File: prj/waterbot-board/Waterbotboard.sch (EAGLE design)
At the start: 63 parts, among them J1 54602-908LF, J2 54602-908LF, U1 MCP4725A0T-E/CHSOT-23-6_MC-L, U2 R-78E5.0-1.0, U3 PCA9615, U4 PCA9615

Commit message: Added boards
waterbot board, relay board
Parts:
- removed D1: SBR2A40P1-7, openag-diodes:SBR2A40P1-7
- removed D2: APT1608, openag-diodes:APT1608CGCK
- removed F1: (no value), fuse:GSH15
- removed J2: 54602-908LF, openag-connectors:RJ45-DI2C-USB-54602-908LFPTH
- removed R1, R19: 100, openag-resistors:100OHM-RC0603JR-07100RL
- removed R13, R14, R15, R16: 600, openag-resistors:600OHM-RC0603FR-07604RL
- removed R17, R18: 120, openag-resistors:120OHM-RC0603FR-07120RL
- removed RELAY_1: G5LE-14_DC12, relay_2:G5LE-14_DC12
- removed TP1, TP12: PTR1B2,54, testpad:PTR1B2,54
- removed TP28, TP3: TPTP06R, openag-testpads:TPTP06R
- removed U$9: LTV-355T, openag-transistors:LTV-355T
- removed U1: MCP4725A0T-E/CHSOT-23-6_MC-L, openag-dacs:MCP4725A0T-E/CHSOT-23-6_MC-L
- removed U4: PCA9615, openag-buffers:PCA9615DPJ
- added C6, C8: 0.1uF, openag-capacitors:0.1UF-C0603C104K5RACTU
- added C7: 4.7uF, openag-capacitors:4.7UF-CL21A475KBQNNNE
- added D10: APT1608, openag-diodes:APT1608CGCK
- added D11: SMAJ26A, openag-diodes:SMAJ26A-13-F
- added D3, D5, D7, D8, D9: SBR2A40P1-7, openag-diodes:SBR2A40P1-7
- added F2, F3, F4, F5, F6: (no value), fuse:GSH15
- added F8: GSH15, openag-fuses:GSH15
- added F9: Use 5A Fuse, openag-fuses:0217005.MXP
- added J4: PJ-036AH, openag-connectors:BARREL-JACK-PJ-036AH-SMT-TR
- added LSP1, LSP10, LSP11, LSP12, LSP13, LSP14, LSP15, LSP2, LSP3, LSP4, LSP5, LSP6, LSP7, LSP8, LSP9: LSP13, solpad:LSP13
- added R20, R21, R22, R23, R24: 100, openag-resistors:100OHM-RC0603JR-07100RL
- added R34, R36, R37, R38, R39, R40, R41, R42: 1K, openag-resistors:1K-ERJ-PB3D1001V
- added R35: 0 OHM, openag-resistors:0OHM-RC0603JR-070RL
- added RELAY_2, RELAY_3, RELAY_4, RELAY_5, RELAY_6: G5LE-14_DC12, relay_2:G5LE-14_DC12
- added SJ_A1, SJ_A2: (no value), openag-connectors:SOLDERJUMPERREFLOW_NOPASTE
- added TP24, TP25, TP26, TP29, TP30, TP31, TP35, TP36, TP37, TP38, TP39, TP40: TPTP04R, openag-testpads:TPTP04R
- added U$10, U$11, U$12, U$13, U$14: LTV-355T, openag-transistors:LTV-355T
- added U5: DAC5578, openag-dacs:DAC5578SPW
- C5: value 0.1uF -> 4.7uF; device openag-capacitors:0.1UF-C0603C104K5RACTU -> openag-capacitors:4.7UF-CL21A475KBQNNNE
- R2: value 100 -> 1K; device openag-resistors:100OHM-RC0603JR-07100RL -> openag-resistors:1K-ERJ-PB3D1001V
- TP27: value TPTP06R -> TPTP04R; device openag-testpads:TPTP06R -> openag-testpads:TPTP04R
- U$6: AUTHOR Dan Poitrast -> Sebastian
- U$7: TITLE LED-DRV -> Water Bot Control Board; URL github.com/openaginitiative/openag-body/prj/usb-hub -> github.com/openaginitiative/openag-body/prj/
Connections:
- removed net DSCLM_2: J2.DSCLM, R15.2, R17.1, U4.DSCLM
- removed net DSCLP_2: J2.DSCLP, R16.1, R17.2, U4.DSCLP
- removed net DSDAM_2: J2.DSDAM, R13.1, R18.2, U4.DSDAM
- removed net DSDAP_3: J2.DSDAP, R14.2, R18.1, U4.DSDAP
- new net !LDAC!: R35.2, R36.2, TP37.TP, U5.!LDAC!
- new net 24V_IN1: F8.1, J4.1
- new net ADDR0: SJ_A1.2, SJ_A2.2, U5.ADDR0
- new net DAC_!CLR!: R34.2, TP38.TP, U5.!CLR!
- new net DIM1: R37.1, U5.VOUT_G
- new net DIM2: R20.1, R38.1, U5.VOUT_E
- new net DIM3: R21.1, R39.1, U5.VOUT_C
- new net DIM4: R22.1, R40.1, U5.VOUT_A
- new net DIM5: R23.1, R41.1, U5.VOUT_H
- new net DIM6: R24.1, R42.1, U5.VOUT_F
- new net N$42: D3.+, RELAY_2.1, U$10.COLLECTOR
- new net N$44: F2.2, RELAY_2.2
- new net N$45: LSP3.MP, RELAY_2.3
- new net N$46: LSP12.MP, RELAY_6.4
- new net N$47: R20.2, U$10.ANODE
- new net N$48: D5.+, RELAY_3.1, U$11.COLLECTOR
- new net N$49: F3.2, RELAY_3.2
- new net N$50: LSP5.MP, RELAY_3.3
- new net N$51: LSP14.MP, RELAY_5.4
- new net N$52: R21.2, U$11.ANODE
- new net N$53: D7.+, RELAY_4.1, U$12.COLLECTOR
- new net N$54: F4.2, RELAY_4.2
- new net N$55: LSP8.MP, RELAY_4.3
- new net N$57: R22.2, U$12.ANODE
- new net N$58: D8.+, RELAY_5.1, U$13.COLLECTOR
- new net N$59: F5.2, RELAY_5.2
- new net N$60: LSP13.MP, RELAY_5.3
- new net N$61: D10.A, R2.1
- new net N$62: R23.2, U$13.ANODE
- new net N$63: D9.+, RELAY_6.1, U$14.COLLECTOR
- new net N$64: F6.2, RELAY_6.2
- new net N$65: LSP11.MP, RELAY_6.3
- new net N$67: R24.2, U$14.ANODE
- new net N$7: F3.1, LSP6.MP
- new net SCL: TP36.TP, U5.SCL
- new net SDA: TP35.TP, U5.SDA
- net +24V: now also C5.1, C8.1, D11.P$2, D3.-, D5.-, D7.-, D8.-, D9.-, F8.2, R2.2, RELAY_2.5, RELAY_3.5, RELAY_4.5, RELAY_5.5, RELAY_6.5, TP24.TP, TP27.TP, TP29.TP; no longer D1.-, J2.+24V, RELAY_1.5, TP3.TP
- net +3V3: now also C6.1, C7.1, R34.1, R36.1, R37.2, R38.2, R39.2, R40.2, R41.2, R42.2, SJ_A1.1, TP30.TP, U5.AVDD, U5.VREF_IN; no longer U4.VDD_(A)
- net +5V: no longer R14.1, R16.2, TP27.TP, U1.VDD, U4.VDD_(B)
- net 24V_EMI: no longer R1.2
- net GND: now also C5.2, C6.2, C7.2, C8.2, D10.C, D11.P$1, J1.GND, J4.2, J4.3, R35.1, SJ_A2.1, TP25.TP, TP26.TP, TP31.TP, TP39.TP, TP40.TP, U$10.CATHODE, U$10.EMITTER, U$11.CATHODE, U$11.EMITTER, U$12.CATHODE, U$12.EMITTER, U$13.CATHODE, U$13.EMITTER, U$14.CATHODE, U$14.EMITTER, U5.GND; no longer D2.C, R13.2, R15.1, R19.1, TP28.TP, U$9.CATHODE, U$9.EMITTER, U1.VSS, U4.VSS
- net N$11: now also F4.1, LSP9.MP; no longer F1.2, RELAY_1.2
- net N$27: now also LSP2.MP, RELAY_2.4; no longer R2.2, U$9.ANODE
- net N$31: now also LSP4.MP, RELAY_3.4; no longer R2.1, U1.VOUT
- net N$32: now also LSP7.MP, RELAY_4.4; no longer R19.2, U1.A0
- net N$4: now also F2.1, LSP1.MP; no longer RELAY_1.3
- net N$5: now also F5.1, LSP15.MP; no longer D1.+, RELAY_1.1, U$9.COLLECTOR
- net N$6: now also F6.1, LSP10.MP; no longer D2.A, R1.1
- net SCL_IN: no longer U1.SCL, U4.SCL
- net SDA_IN: no longer U1.SDA, U4.SDA
- net USBM: no longer J2.USBM
- net USBP: no longer J2.USBP
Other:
- note added: "24V Power Conditioning"
- note added: "8-Channel 8-Bit I2C DAC"
- note added: "Barrel Jack Connector"
- note added: "Barrel Jack Connector with 24V Conditioning + Fuse + Indicator LED"
- note added: "DAC Address Set"
- note added: "DAC HW Enable"
- note added: "DAC Signal Pullups"
- note added: "Note: - Barrel jack rated for 5A"
- note added: "Notes: - GND !LDAC! for syncronous mode - Broadcast I2C Addr = 0x47 - ADDR0=Low, I2C Addr=0x48 - ADDR0=High, I2C Addr=0x4A - ADDR0=Float, I2C Addr=0x4C"
- note removed: "dI2C Buffer Channel 2"
- moved on the sheet: C3, TP27

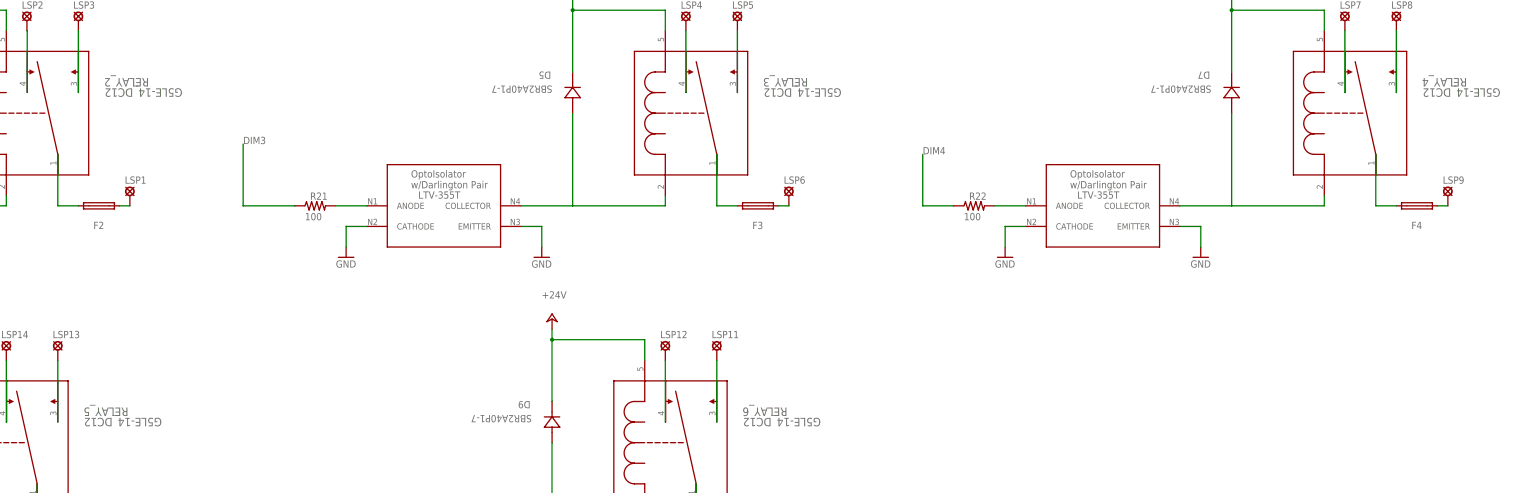
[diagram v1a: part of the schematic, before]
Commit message: Added RJ45 adapter and more
Added boards
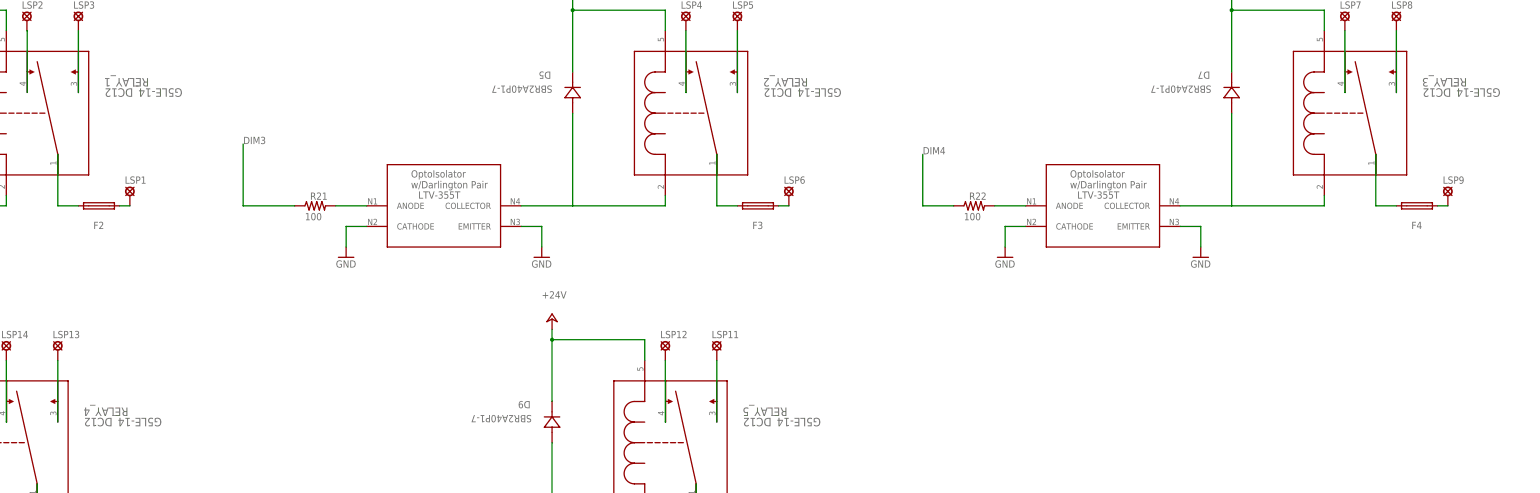
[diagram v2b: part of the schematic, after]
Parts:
- removed RELAY_6: G5LE-14_DC12, relay_2:G5LE-14_DC12
- added RELAY_1: G5LE-14_DC12, relay_2:G5LE-14_DC12
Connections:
- net +24V: now also RELAY_1.5; no longer RELAY_6.5
- net N$27: now also RELAY_1.4; no longer RELAY_2.4
- net N$31: now also RELAY_2.4; no longer RELAY_3.4
- net N$32: now also RELAY_3.4; no longer RELAY_4.4
- net N$42: now also RELAY_1.1; no longer RELAY_2.1
- net N$44: now also RELAY_1.2; no longer RELAY_2.2
- net N$45: now also RELAY_1.3; no longer RELAY_2.3
- net N$46: now also RELAY_5.4; no longer RELAY_6.4
- net N$48: now also RELAY_2.1; no longer RELAY_3.1
- net N$49: now also RELAY_2.2; no longer RELAY_3.2
- net N$50: now also RELAY_2.3; no longer RELAY_3.3
- net N$51: now also RELAY_4.4; no longer RELAY_5.4
- net N$53: now also RELAY_3.1; no longer RELAY_4.1
- net N$54: now also RELAY_3.2; no longer RELAY_4.2
- net N$55: now also RELAY_3.3; no longer RELAY_4.3
- net N$58: now also RELAY_4.1; no longer RELAY_5.1
- net N$59: now also RELAY_4.2; no longer RELAY_5.2
- net N$60: now also RELAY_4.3; no longer RELAY_5.3
- net N$63: now also RELAY_5.1; no longer RELAY_6.1
- net N$64: now also RELAY_5.2; no longer RELAY_6.2
- net N$65: now also RELAY_5.3; no longer RELAY_6.3
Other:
- moved on the sheet: RELAY_2, RELAY_3, RELAY_4, RELAY_5

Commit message: added fermentaboard, etc
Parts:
- added TP1, TP12, TP3: TPB2,54, testpad:TPB2,54
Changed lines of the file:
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@@
 <part name="TP27" library="openag-testpads" deviceset="TP" device="TP04R"/>
 <part name="F9" library="openag-fuses" library_urn="urn:adsk.eagle:library:4908427" deviceset="0217005.MXP" device="" package3d_urn="urn:adsk.eagle:package:4908436/1" value="Use 5A Fuse"/>
+<part name="TP1" library="testpad" library_urn="urn:adsk.eagle:library:385" deviceset="TP" device="B2,54" package3d_urn="urn:adsk.eagle:package:27948/1"/>
+<part name="TP3" library="testpad" library_urn="urn:adsk.eagle:library:385" deviceset="TP" device="B2,54" package3d_urn="urn:adsk.eagle:package:27948/1"/>
+<part name="TP12" library="testpad" library_urn="urn:adsk.eagle:library:385" deviceset="TP" device="B2,54" package3d_urn="urn:adsk.eagle:package:27948/1"/>
 </parts>
 <sheets>
@@
 <attribute name="NAME" x="-83.82" y="185.42" size="1.778" layer="95"/>
 </instance>
+<instance part="TP1" gate="G$1" x="-452.12" y="-25.4" smashed="yes">
+<attribute name="NAME" x="-453.39" y="-24.13" size="1.778" layer="95"/>
+<attribute name="TP_SIGNAL_NAME" x="-450.85" y="-26.67" size="1.778" layer="97"/>
+</instance>
+<instance part="TP3" gate="G$1" x="-452.12" y="-15.24" smashed="yes">
+<attribute name="NAME" x="-453.39" y="-13.97" size="1.778" layer="95"/>
+<attribute name="TP_SIGNAL_NAME" x="-450.85" y="-16.51" size="1.778" layer="97"/>
+</instance>
+<instance part="TP12" gate="G$1" x="-452.12" y="-5.08" smashed="yes">
+<attribute name="NAME" x="-453.39" y="-3.81" size="1.778" layer="95"/>
+<attribute name="TP_SIGNAL_NAME" x="-450.85" y="-6.35" size="1.778" layer="97"/>
+</instance>
 </instances>
